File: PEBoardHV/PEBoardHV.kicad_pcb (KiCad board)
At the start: 2 copper layers, 106.7 x 76.2 mm, 45 parts, among them J1 To PE LV, J2 Left Connector (Master), J3 E-Meter Internal, J4 Right Connector (Slave), J5 E-Meter External, J6 HV Cable, J7 TSMPs, J8 HV CAN Debug, J9 EMeter HV, U1 L78S05CV-DG, U2 ISO1050, U3 PS2501-4, U4 DK1A1B-12V, U5 DK1A1B-12V

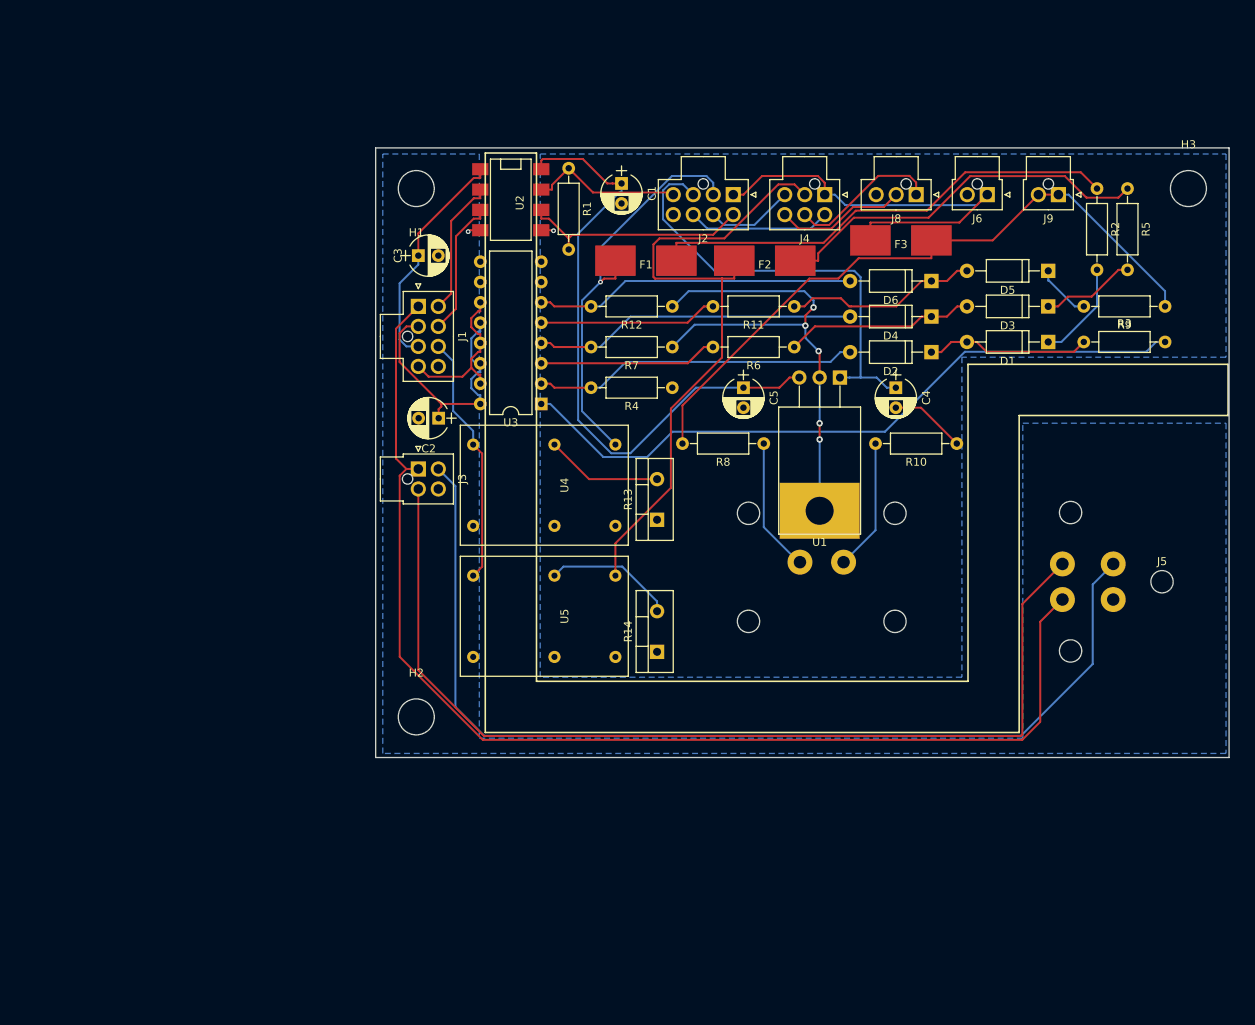
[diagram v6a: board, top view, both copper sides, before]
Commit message: Fix drill sizes for manufacturing on PE HV board
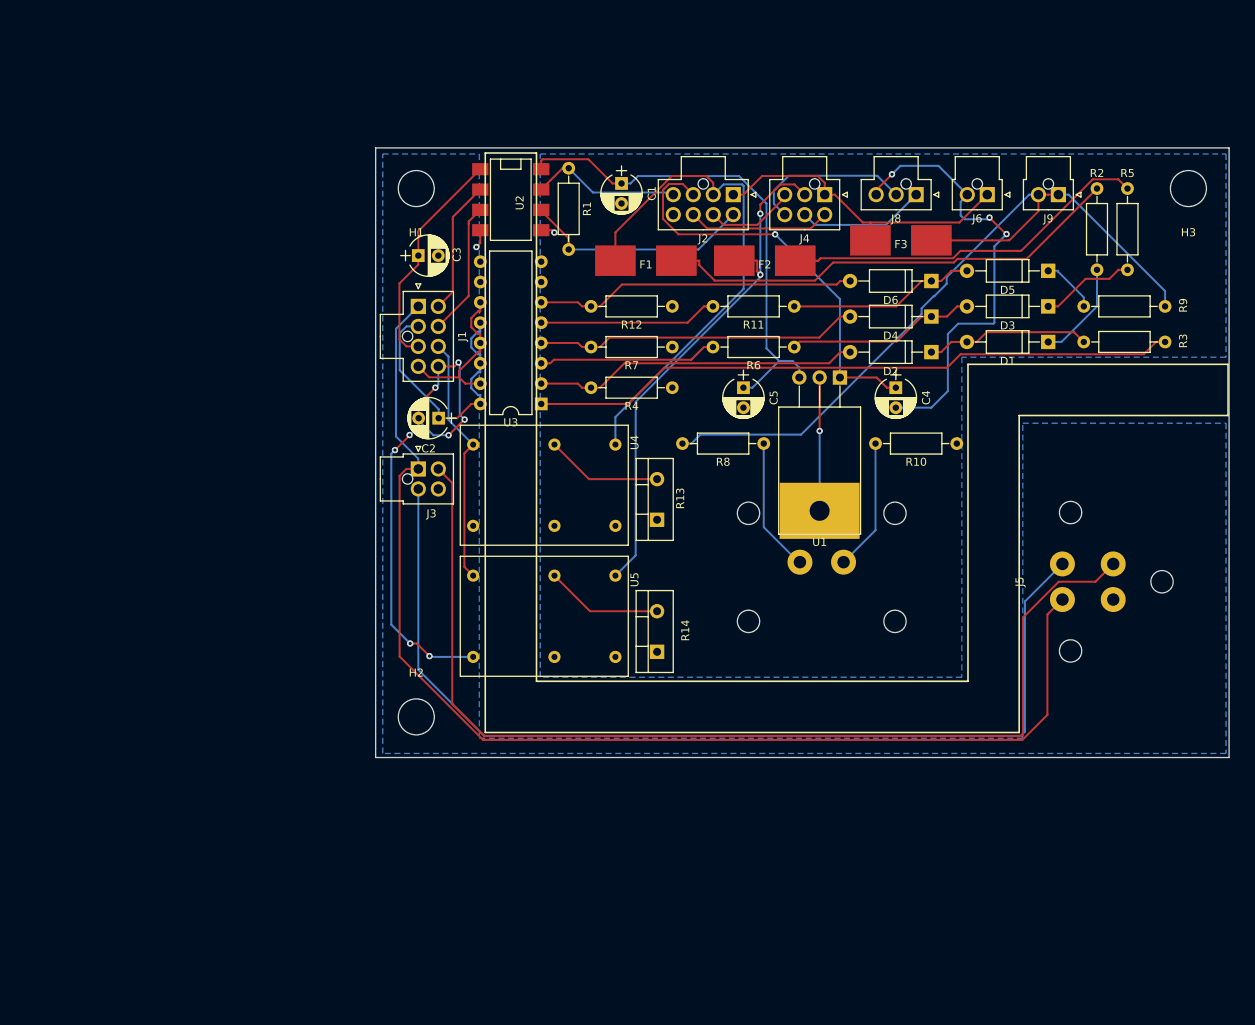
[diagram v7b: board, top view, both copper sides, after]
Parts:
- turned H3 to 180 degrees
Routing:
- net GND: track 1.59 -> 66.7 mm, vias 1 -> 9
- net /TS+_SWITCHED_R: track 81.7 -> 65.8 mm, vias 0 -> 2
- net /5V_TS: track 77.8 -> 62.7 mm
- net /TS+: track 53.9 -> 39.7 mm
- net /TS+_FUSED: track 84.2 -> 98.0 mm
- net /TS+_SWITCHED_L: track 51.2 -> 63.9 mm, vias 1 -> 0
- net Net-(R3-Pad2): track 86.7 -> 81.2 mm
- net /CAN_L_DEBUG: track 16.4 -> 20.6 mm
- net /CAN+: track 56.0 -> 51.8 mm, vias 0 -> 1
- net /CAN_H_DEBUG: track 18.9 -> 16.0 mm
- net /EM_SIG-: track 129.1 -> 131.8 mm
- net Net-(F2-Pad2): track 48.0 -> 46.2 mm
- net Net-(R14-Pad2): track 16.3 -> 14.7 mm
- net /CAN_L_BOARD: track 28.7 -> 30.1 mm
- net Net-(D5-Pad2): track 24.3 -> 23.4 mm
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
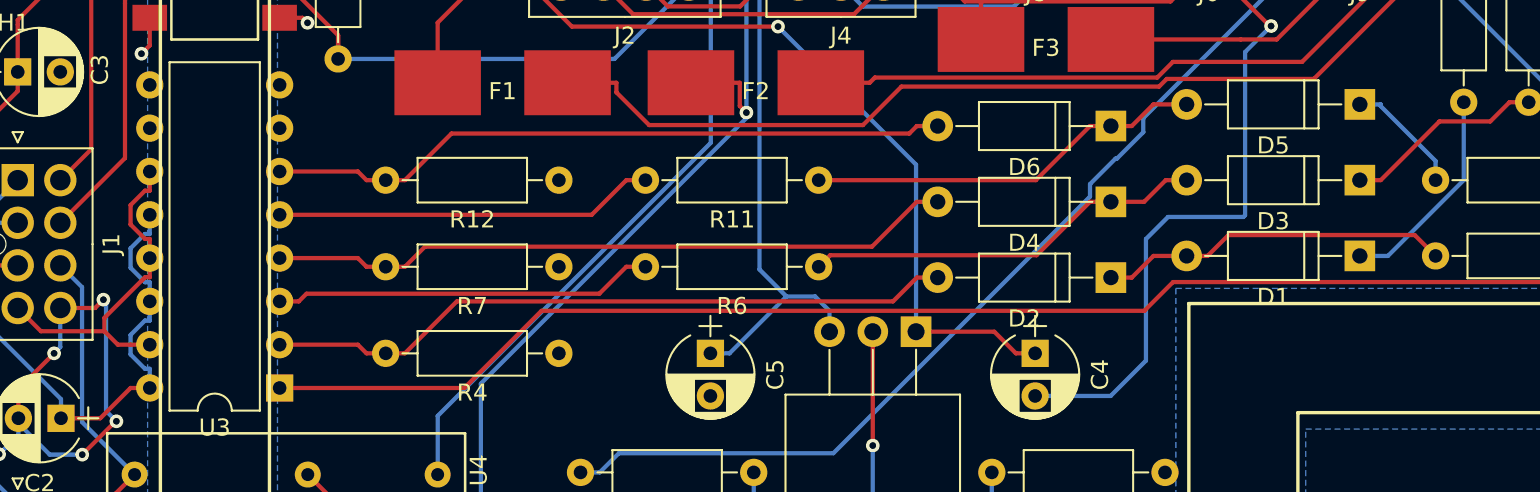
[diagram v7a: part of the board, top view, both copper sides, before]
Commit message: Tweak routing on boards, add mounting holes to dash switchbox
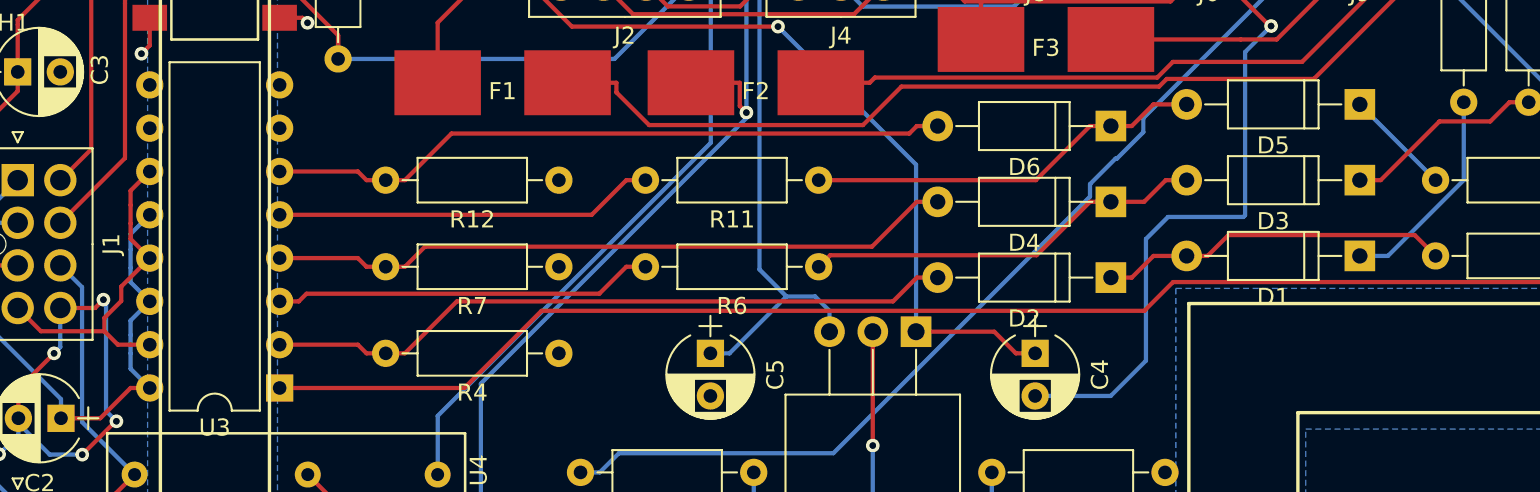
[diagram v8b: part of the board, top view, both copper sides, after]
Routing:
- net Net-(D5-Pad1): track 7.00 -> 6.29 mm
- net /5V_GLV: track 33.9 -> 33.3 mm
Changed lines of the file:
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@@
     (thickness 1.6)
     (drawings 14)
-    (tracks 362)
+    (tracks 353)
     (zones 0)
     (modules 45)
@@
   (gr_line (start 140.5 117.983) (end 194.437 117.983) (angle 90) (layer F.SilkS) (width 0.2))
   (gr_line (start 140.5 51.943) (end 140.5 117.983) (angle 90) (layer F.SilkS) (width 0.2))
+  (segment (start 132.3517 75.184) (end 132.3517 74.2773) (width 0.25) (layer B.Cu) (net 1))
+  (segment (start 132.3517 74.2773) (end 133.477 73.152) (width 0.25) (layer B.Cu) (net 1) (status 800000))
+  (segment (start 132.3517 76.2628) (end 132.3517 77.1067) (width 0.25) (layer B.Cu) (net 1))
+  (segment (start 132.3517 77.1067) (end 133.477 78.232) (width 0.25) (layer B.Cu) (net 1) (status 800000))
+  (segment (start 132.3517 80.2012) (end 132.3517 79.3573) (width 0.25) (layer B.Cu) (net 1))
+  (segment (start 132.3517 79.3573) (end 133.477 78.232) (width 0.25) (layer B.Cu) (net 1) (status 800000))
+  (segment (start 132.3517 81.28) (end 132.3517 82.1867) (width 0.25) (layer B.Cu) (net 1))
+  (segment (start 132.3517 82.1867) (end 133.477 83.312) (width 0.25) (layer B.Cu) (net 1) (status 800000))
+  (segment (start 132.3517 81.28) (end 132.3517 80.2012) (width 0.25) (layer B.Cu) (net 1))
   (segment (start 123.4092 79.1039) (end 128.27 83.9647) (width 0.25) (layer B.Cu) (net 1))
   (segment (start 123.4092 74.4594) (end 123.4092 79.1039) (width 0.25) (layer B.Cu) (net 1))
@@
   (segment (start 128.27 85.09) (end 128.27 83.9647) (width 0.25) (layer B.Cu) (net 1))
   (segment (start 130.5737 85.09) (end 132.3517 83.312) (width 0.25) (layer F.Cu) (net 1))
+  (segment (start 133.477 83.312) (end 132.3517 83.312) (width 0.25) (layer F.Cu) (net 1))
   (segment (start 128.27 85.09) (end 130.5737 85.09) (width 0.25) (layer F.Cu) (net 1))
-  (segment (start 133.477 83.312) (end 132.3517 83.312) (width 0.25) (layer F.Cu) (net 1))
-  (segment (start 133.1956 74.2773) (end 133.477 74.2773) (width 0.25) (layer B.Cu) (net 1))
-  (segment (start 132.3517 75.1212) (end 133.1956 74.2773) (width 0.25) (layer B.Cu) (net 1))
-  (segment (start 132.3517 76.2628) (end 132.3517 75.1212) (width 0.25) (layer B.Cu) (net 1))
-  (segment (start 133.1956 77.1067) (end 132.3517 76.2628) (width 0.25) (layer B.Cu) (net 1))
-  (segment (start 133.477 77.1067) (end 133.1956 77.1067) (width 0.25) (layer B.Cu) (net 1))
-  (segment (start 133.477 73.152) (end 133.477 74.2773) (width 0.25) (layer B.Cu) (net 1))
-  (segment (start 133.477 78.232) (end 133.477 77.1067) (width 0.25) (layer B.Cu) (net 1))
-  (segment (start 133.1956 79.3573) (end 133.477 79.3573) (width 0.25) (layer B.Cu) (net 1))
-  (segment (start 132.3517 80.2012) (end 133.1956 79.3573) (width 0.25) (layer B.Cu) (net 1))
-  (segment (start 132.3517 81.3427) (end 132.3517 80.2012) (width 0.25) (layer B.Cu) (net 1))
-  (segment (start 133.1957 82.1867) (end 132.3517 81.3427) (width 0.25) (layer B.Cu) (net 1))
-  (segment (start 133.477 82.1867) (end 133.1957 82.1867) (width 0.25) (layer B.Cu) (net 1))
-  (segment (start 133.477 83.312) (end 133.477 82.1867) (width 0.25) (layer B.Cu) (net 1))
-  (segment (start 133.477 78.232) (end 133.477 79.3573) (width 0.25) (layer B.Cu) (net 1))
+  (segment (start 132.3517 76.2628) (end 132.3517 75.184) (width 0.25) (layer B.Cu) (net 1))
   (segment (start 125.77 85.09) (end 125.77 85.384) (width 0.25) (layer B.Cu) (net 2))
   (segment (start 125.77 85.384) (end 127.6096 87.2236) (width 0.25) (layer B.Cu) (net 2))
@@
   (segment (start 175.8495 75.0202) (end 149.625 75.0202) (width 0.25) (layer F.Cu) (net 12))
   (segment (start 178.4797 72.39) (end 175.8495 75.0202) (width 0.25) (layer F.Cu) (net 12))
-  (segment (start 205.6953 66.775) (end 208.915 69.9947) (width 0.25) (layer B.Cu) (net 13))
-  (segment (start 205.6953 66.675) (end 205.6953 66.775) (width 0.25) (layer B.Cu) (net 13))
-  (segment (start 204.47 66.675) (end 205.6953 66.675) (width 0.25) (layer B.Cu) (net 13))
-  (segment (start 208.915 71.12) (end 208.915 69.9947) (width 0.25) (layer B.Cu) (net 13))
+  (segment (start 204.47 66.675) (end 208.915 71.12) (width 0.25) (layer B.Cu) (net 13))
   (segment (start 185.4647 71.12) (end 172.72 71.12) (width 0.25) (layer F.Cu) (net 14))
   (segment (start 188.6397 67.945) (end 185.4647 71.12) (width 0.25) (layer F.Cu) (net 14))
@@
   (segment (start 124.2429 91.44) (end 123.3841 92.2988) (width 0.25) (layer F.Cu) (net 22))
   (segment (start 125.73 91.44) (end 124.2429 91.44) (width 0.25) (layer F.Cu) (net 22))
+  (segment (start 131.8035 78.2095) (end 131.8035 77.3655) (width 0.25) (layer F.Cu) (net 23))
+  (segment (start 131.8035 77.3655) (end 133.477 75.692) (width 0.25) (layer F.Cu) (net 23))
+  (segment (start 132.3517 73.66) (end 132.3517 74.5667) (width 0.25) (layer F.Cu) (net 23))
+  (segment (start 132.3517 73.66) (end 132.3517 72.5812) (width 0.25) (layer F.Cu) (net 23))
+  (segment (start 132.3517 71.7373) (end 133.477 70.612) (width 0.25) (layer F.Cu) (net 23))
+  (segment (start 132.3517 72.5812) (end 132.3517 71.7373) (width 0.25) (layer F.Cu) (net 23))
+  (segment (start 132.3517 74.5667) (end 133.477 75.692) (width 0.25) (layer F.Cu) (net 23))
   (segment (start 133.477 80.772) (end 132.3517 80.772) (width 0.25) (layer F.Cu) (net 23))
-  (segment (start 133.1956 71.7373) (end 133.477 71.7373) (width 0.25) (layer F.Cu) (net 23))
-  (segment (start 132.3517 72.5812) (end 133.1956 71.7373) (width 0.25) (layer F.Cu) (net 23))
-  (segment (start 132.3517 73.7227) (end 132.3517 72.5812) (width 0.25) (layer F.Cu) (net 23))
-  (segment (start 133.1957 74.5667) (end 132.3517 73.7227) (width 0.25) (layer F.Cu) (net 23))
-  (segment (start 133.477 74.5667) (end 133.1957 74.5667) (width 0.25) (layer F.Cu) (net 23))
-  (segment (start 133.477 75.692) (end 133.477 74.5667) (width 0.25) (layer F.Cu) (net 23))
-  (segment (start 133.477 70.612) (end 133.477 71.7373) (width 0.25) (layer F.Cu) (net 23))
-  (segment (start 133.477 75.692) (end 133.477 76.8173) (width 0.25) (layer F.Cu) (net 23))
   (segment (start 127.0945 79.9845) (end 125.73 78.62) (width 0.25) (layer F.Cu) (net 23))
   (segment (start 130.8159 79.9845) (end 127.0945 79.9845) (width 0.25) (layer F.Cu) (net 23))
   (segment (start 131.6034 80.772) (end 130.8159 79.9845) (width 0.25) (layer F.Cu) (net 23))
   (segment (start 132.3517 80.772) (end 131.6034 80.772) (width 0.25) (layer F.Cu) (net 23))
-  (segment (start 133.1957 76.8173) (end 133.477 76.8173) (width 0.25) (layer F.Cu) (net 23))
-  (segment (start 130.8159 79.1971) (end 133.1957 76.8173) (width 0.25) (layer F.Cu) (net 23))
+  (segment (start 130.8159 79.1971) (end 131.8035 78.2095) (width 0.25) (layer F.Cu) (net 23))
   (segment (start 130.8159 79.9845) (end 130.8159 79.1971) (width 0.25) (layer F.Cu) (net 23))
   (segment (start 132.0244 60.7794) (end 132.0244 60.5076) (width 0.25) (layer F.Cu) (net 24))
